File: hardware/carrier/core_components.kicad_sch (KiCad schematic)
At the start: 52 parts, among them J1 PANEL, J2 CARDKB, J3 HAPTIC, J4 EXT_LED, J5 PIEZ, M1 Walter, Q1 UMH3N, Q2 SI1308EDL, Q3 MMST3904, SW1 KMR221GLFS, U1 CP2102N-A02-GQFN24, U2 SN74LVC2G126DCUR, U3 DRV2605LDGSR, U4 LIS2DW12TR

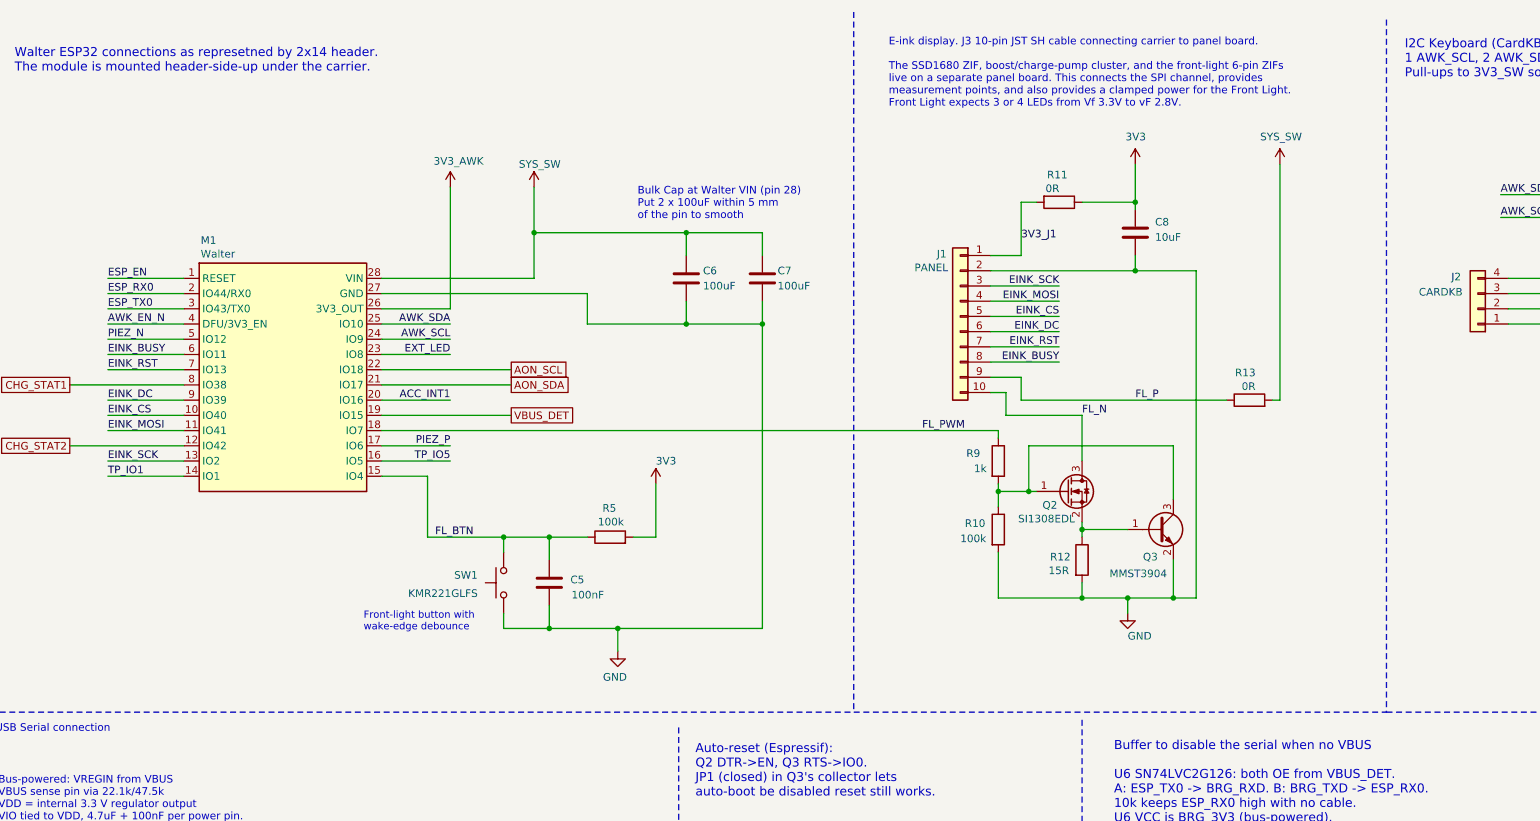
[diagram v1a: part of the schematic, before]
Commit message: Carrier: hand-layout WIP, Walter pins remapped, panel header J1 10 -> 8 pins (owner)
Co-Authored-By: Claude Fable 5.1 <noreply@anthropic.com>
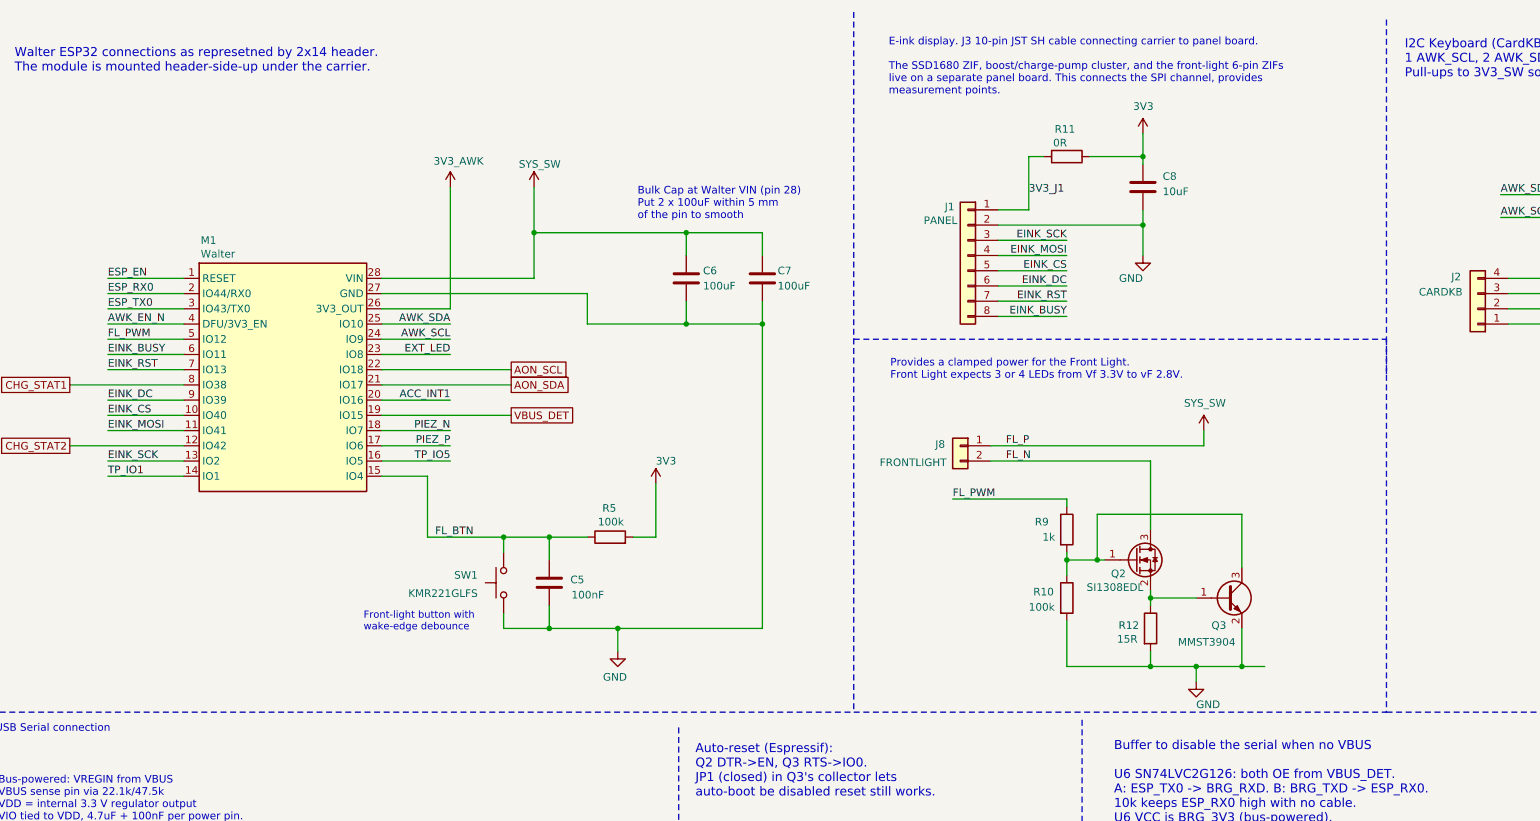
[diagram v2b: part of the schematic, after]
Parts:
- removed J1: PANEL, Connector_JST:JST_SH_SM10B-SRSS-TB_1x10-1MP_P1.00mm_Horizontal, symbol Connector_Generic:Conn_01x10
- removed R13: 0R, Resistor_SMD:R_0402_1005Metric, symbol Device:R
- added J1: PANEL, Connector_JST:JST_SH_SM08B-SRSS-TB_1x08-1MP_P1.00mm_Horizontal, symbol Connector_Generic:Conn_01x08
- added J8: FRONTLIGHT, Connector_JST:JST_SH_SM02B-SRSS-TB_1x02-1MP_P1.00mm_Horizontal, symbol Connector_Generic:Conn_01x02
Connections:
- net 3V3_J1: now also J1.1 (Pin_1)
- net EINK_BUSY: now also J1.8 (Pin_8)
- net EINK_CS: now also J1.5 (Pin_5)
- net EINK_DC: now also J1.6 (Pin_6)
- net EINK_MOSI: now also J1.4 (Pin_4)
- net EINK_RST: now also J1.7 (Pin_7)
- net EINK_SCK: now also J1.3 (Pin_3)
- net FL_N: now also J8.2 (Pin_2)
- net FL_PWM: now also M1.5 (IO12); no longer M1.18 (IO7)
- net GND: now also J1.2 (Pin_2)
- net PIEZ_N: now also M1.18 (IO7); no longer M1.5 (IO12)
- net SYS_SW: now also J8.1 (Pin_1)
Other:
- note added: "E-ink display. J3 10-pin JST SH cable connecting carrier to panel board. The SSD1680 ZIF, boost/charge-pump cluster, and the front-light 6-pin ZIFs live on a separate panel board. This connects the SPI channel, provides measurement points."
- note added: "Provides a clamped power for the Front Light. Front Light expects 3 or 4 LEDs from Vf 3.3V to vF 2.8V."
- note removed: "E-ink display. J3 10-pin JST SH cable connecting carrier to panel board. The SSD1680 ZIF, boost/charge-pump cluster, and the front-light 6-pin ZIFs live on a separate panel board. This connects the SPI channel, provides measurement points, and also provides a clamped power for the Front Light. Front Light expects 3 or 4 LEDs from Vf 3.3V to vF 2.8V."
- moved on the sheet: C8, Q2, Q3, R10, R11, R12, R9
